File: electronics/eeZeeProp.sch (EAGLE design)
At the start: 34 parts, among them Q1 5MHz, Q2 2N3904SOT23, SW1 RESET, U1 P8X32A-Q44, U2 24LC256-I/ST, U3 NCP1117 3V3

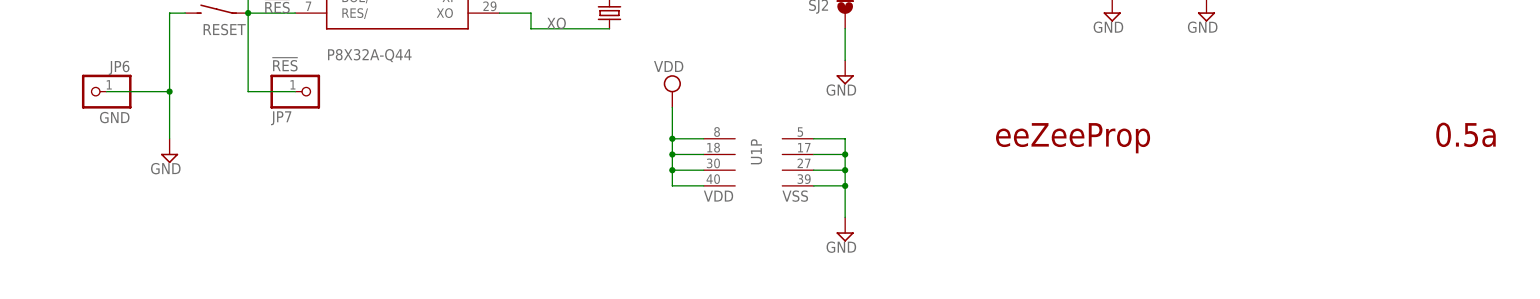
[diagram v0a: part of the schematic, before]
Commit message: Revised silkscreen labels, added user guide link, minor relocation of 3v3 ftdi solder jumper and label, updated bt logo
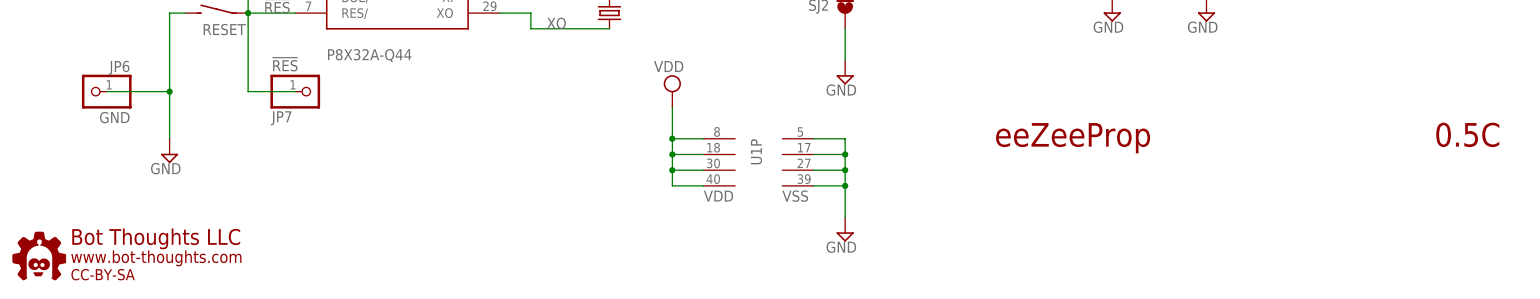
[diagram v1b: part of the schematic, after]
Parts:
- added U$1: BTLOGO-LOGO-MD, bt:BTLOGO-LOGO-MD
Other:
- note added: "0.5C"
- note removed: "0.5a"
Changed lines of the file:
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@@
 <?xml version="1.0" encoding="utf-8"?>
 <!DOCTYPE eagle SYSTEM "eagle.dtd">
-<eagle version="6.4">
+<eagle version="7.1.0">
 <drawing>
 <settings>
@@
 <layer number="54" name="bGND_GNDA" color="1" fill="9" visible="no" active="no"/>
 <layer number="56" name="wert" color="7" fill="1" visible="no" active="no"/>
+<layer number="57" name="tCAD" color="7" fill="1" visible="no" active="no"/>
+<layer number="59" name="tCarbon" color="7" fill="1" visible="no" active="no"/>
+<layer number="60" name="bCarbon" color="7" fill="1" visible="no" active="no"/>
+<layer number="90" name="Modules" color="5" fill="1" visible="no" active="no"/>
 <layer number="91" name="Nets" color="2" fill="1" visible="yes" active="yes"/>
 <layer number="92" name="Busses" color="1" fill="1" visible="yes" active="yes"/>
@@
 <layer number="97" name="Info" color="7" fill="1" visible="yes" active="yes"/>
 <layer number="98" name="Guide" color="6" fill="1" visible="yes" active="yes"/>
+<layer number="99" name="SpiceOrder" color="7" fill="1" visible="no" active="no"/>
 <layer number="100" name="Muster" color="7" fill="1" visible="no" active="no"/>
 <layer number="101" name="Patch_Top" color="12" fill="4" visible="yes" active="yes"/>
@@
 <layer number="106" name="bPlate" color="7" fill="1" visible="yes" active="yes"/>
 <layer number="107" name="Crop" color="7" fill="1" visible="yes" active="yes"/>
+<layer number="108" name="tplace-old" color="10" fill="1" visible="no" active="yes"/>
+<layer number="109" name="ref-old" color="11" fill="1" visible="no" active="yes"/>
+<layer number="110" name="fp0" color="7" fill="1" visible="no" active="yes"/>
+<layer number="111" name="LPC17xx" color="7" fill="1" visible="no" active="yes"/>
+<layer number="112" name="tSilk" color="7" fill="1" visible="no" active="yes"/>
+<layer number="113" name="IDFDebug" color="4" fill="1" visible="no" active="yes"/>
 <layer number="116" name="Patch_BOT" color="9" fill="4" visible="yes" active="yes"/>
 <layer number="121" name="_tsilk" color="7" fill="1" visible="yes" active="yes"/>
 <layer number="122" name="_bsilk" color="7" fill="1" visible="yes" active="yes"/>
+<layer number="123" name="tTestmark" color="7" fill="1" visible="no" active="yes"/>
+<layer number="124" name="bTestmark" color="7" fill="1" visible="no" active="yes"/>
 <layer number="125" name="_tNames" color="7" fill="1" visible="no" active="yes"/>
+<layer number="126" name="_bNames" color="7" fill="1" visible="no" active="yes"/>
+<layer number="127" name="_tValues" color="7" fill="1" visible="no" active="yes"/>
+<layer number="128" name="_bValues" color="7" fill="1" visible="no" active="yes"/>
+<layer number="129" name="Mask" color="7" fill="1" visible="no" active="yes"/>
+<layer number="131" name="tAdjust" color="7" fill="1" visible="no" active="yes"/>
+<layer number="132" name="bAdjust" color="7" fill="1" visible="no" active="yes"/>
 <layer number="144" name="Drill_legend" color="7" fill="1" visible="yes" active="yes"/>
+<layer number="150" name="Notes" color="7" fill="1" visible="no" active="yes"/>
 <layer number="151" name="HeatSink" color="7" fill="1" visible="yes" active="yes"/>
+<layer number="152" name="_bDocu" color="7" fill="1" visible="no" active="yes"/>
+<layer number="153" name="FabDoc1" color="7" fill="1" visible="no" active="yes"/>
+<layer number="154" name="FabDoc2" color="7" fill="1" visible="no" active="yes"/>
+<layer number="155" name="FabDoc3" color="7" fill="1" visible="no" active="yes"/>
+<layer number="199" name="Contour" color="7" fill="1" visible="no" active="yes"/>
 <layer number="200" name="200bmp" color="1" fill="10" visible="yes" active="yes"/>
 <layer number="201" name="201bmp" color="2" fill="10" visible="yes" active="yes"/>
@@
 <layer number="223" name="223bmp" color="24" fill="1" visible="no" active="no"/>
 <layer number="224" name="224bmp" color="25" fill="1" visible="no" active="no"/>
+<layer number="225" name="225bmp" color="7" fill="1" visible="no" active="yes"/>
+<layer number="226" name="226bmp" color="7" fill="1" visible="no" active="yes"/>
+<layer number="227" name="227bmp" color="7" fill="1" visible="no" active="yes"/>
+<layer number="228" name="228bmp" color="7" fill="1" visible="no" active="yes"/>
+<layer number="229" name="229bmp" color="7" fill="1" visible="no" active="yes"/>
+<layer number="230" name="230bmp" color="7" fill="1" visible="no" active="yes"/>
 <layer number="231" name="Eagle3D_PG1" color="14" fill="1" visible="yes" active="yes"/>
 <layer number="232" name="Eagle3D_PG2" color="14" fill="2" visible="yes" active="yes"/>
 <layer number="233" name="Eagle3D_PG3" color="14" fill="4" visible="yes" active="yes"/>
+<layer number="248" name="Housing" color="7" fill="1" visible="no" active="yes"/>
+<layer number="249" name="Edge" color="7" fill="1" visible="no" active="yes"/>
 <layer number="250" name="Descript" color="3" fill="1" visible="no" active="no"/>
 <layer number="251" name="SMDround" color="12" fill="11" visible="no" active="no"/>
 <layer number="254" name="cooling" color="7" fill="1" visible="yes" active="yes"/>
+<layer number="255" name="routoute" color="7" fill="1" visible="no" active="yes"/>
 </layers>
 <schematic xreflabel="%F%N/%S.%C%R" xrefpart="/%S.%C%R">
@@
 <part name="SUPPLY13" library="supply2" deviceset="GND" device=""/>
 <part name="SJ3" library="SparkFun" deviceset="SOLDERJUMPER" device="NO" value="3V3FTDI"/>
+<part name="U$1" library="bt" deviceset="BTLOGO" device="-LOGO-MD"/>
 </parts>
 <sheets>
@@
 <text x="43.18" y="48.26" size="1.778" layer="95">!BOE</text>
 <text x="161.29" y="24.13" size="3.81" layer="94">eeZeeProp</text>
-<text x="232.41" y="24.13" size="3.81" layer="94">0.5a</text>
+<text x="232.41" y="24.13" size="3.81" layer="94">0.5C</text>
 <text x="86.36" y="157.48" size="1.778" layer="97">RXI</text>
 <text x="86.36" y="154.94" size="1.778" layer="97">TXO</text>
@@
 <instance part="SUPPLY13" gate="GND" x="137.16" y="35.56" rot="MR0"/>
 <instance part="SJ3" gate="1" x="152.4" y="119.38" rot="R180"/>
+<instance part="U$1" gate="G$1" x="2.54" y="2.54"/>
 </instances>
 <busses>
